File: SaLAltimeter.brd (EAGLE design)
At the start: 100 x 80 mm, 40 parts, among them U1 ATSAMD21G-A, U2 V_REG_LDOSMD, U3 ADXL345

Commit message: added transmiter
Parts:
- added C13: 39pF, SparkFun-Capacitors:0402-CAP
- added C14: 2.2pF, SparkFun-Capacitors:0402-CAP
- added C15, C18, C19: 5.1pF, SparkFun-Capacitors:0402-CAP
- added C16: (no value), SparkFun-Capacitors:0402-CAP
- added C17: 6.2pF, SparkFun-Capacitors:0402-CAP
- added C20, C37: 10nF, SparkFun-Capacitors:0402-CAP
- added C21, C23, C24, C25, C26, C27, C30, C31, C33, C34, C35: 47nF, SparkFun-Capacitors:0402-CAP
- added C22: 1.8nF, SparkFun-Capacitors:0402-CAP
- added C28, C29: 15pF, SparkFun-Capacitors:0402-CAP
- added C32: 220nF, SparkFun-Capacitors:0402-CAP
- added C36: 56pF, SparkFun-Capacitors:0402-CAP
- added C38: 100pF, SparkFun-Capacitors:0402-CAP
- added J$1: SMA_EDGE, SparkFun-Connectors:SMA-EDGE
- added L2, L6: 15nH, SparkFun-Passives:C0402
- added L3: 43nH, SparkFun-Passives:C0402
- added L4: 22nH, SparkFun-Passives:C0402
- added L5, L7: 56nH, SparkFun-Passives:C0402
- added L8, L9: 27nH, SparkFun-Passives:C0402
- added R13, R15: (no value), SparkFun-Passives:0402-RES
- added R14: 0ohm, SparkFun-Passives:0402-RES
- added R16: 56KOhm, SparkFun-Passives:0402-RES
- added S1: SWITCH-MOMENTARY-2SMD-3, SparkFun-Electromechanical:TACTILE_SWITCH_SMD-3
- added U$7: CC1120, SaL-lib:CC1120
- added U4: (no value), adafruit:FGPMMOPA6H
- added Y3: 32MHz, SparkFun-FreqCtrl:CRYSTAL-SMD-5X3
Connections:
- new net CS_TX: U$7.11
- new net N$10: C13.2, C14.1, L2.1
- new net N$11: C14.2, C15.1, L2.2, L3.1
- new net N$12: C16.2, C17.1, L3.2, L4.1
- new net N$13: C16.1, J$1.SIG, L4.2
- new net N$15: C23.2, U$7.25
- new net N$16: C15.2, L6.2, U$7.18
- new net N$17: C18.1, L7.2, L9.1, U$7.19
- new net N$18: C18.2, L6.1, L8.2
- new net N$19: C19.1, L7.1, L8.1, U$7.20
- new net N$20: C22.1, U$7.24
- new net N$21: C22.2, U$7.23
- new net N$22: C20.1, U$7.21
- new net N$23: C24.2, U$7.26
- new net N$24: R16.1, U$7.14
- new net N$25: R14.1, U$7.32
- new net N$26: C27.2, U$7.29
- new net N$27: C29.2, U$7.30, Y3.3
- new net N$28: C28.2, U$7.31, Y3.1
- new net N$34: C32.2, U$7.6
- new net N$38: C36.2, L5.1, R15.1
- new net N$9: C13.1, L5.2, U$7.17
- new net PROG: R13.2, S1.1
- net 3.3V: now also C21.1, C25.2, C26.2, C30.2, C31.2, C33.2, C34.2, C35.2, C36.1, C37.2, C38.2, R15.2, S1.4, U$7.1, U$7.12, U$7.13, U$7.15, U$7.22, U$7.27, U$7.28, U$7.5
- net GND: now also C17.2, C19.2, C20.2, C21.2, C23.1, C24.1, C25.1, C26.1, C27.1, C28.1, C29.1, C30.1, C31.1, C32.1, C33.1, C34.1, C35.1, C37.1, C38.1, J$1.GND@0, J$1.GND@1, J$1.GND@2, J$1.GND@3, L9.2, R13.1, R14.2, R16.2
- net MISO: now also U$7.9
- net MOSI: now also U$7.7
- net SCK: now also U$7.8
- net SWCLK: now also U1.45
- net SWDIO: now also U1.46
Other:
- board size 100 x 80 mm -> 244.8 x 151.1 mm

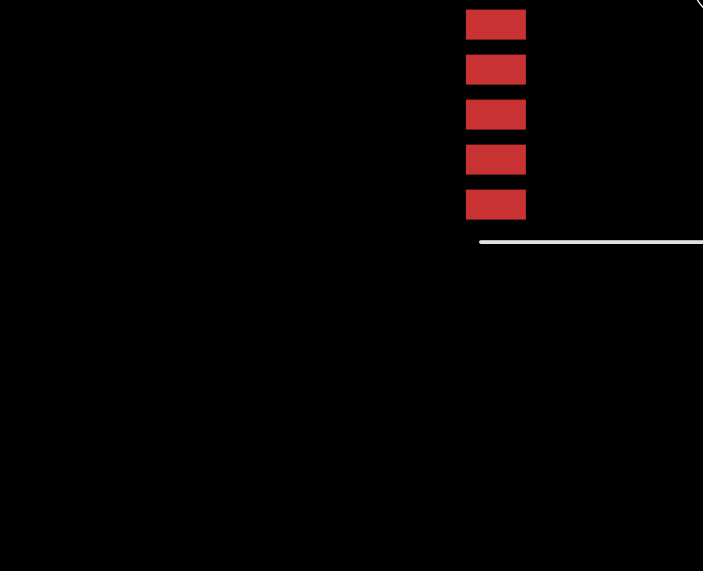
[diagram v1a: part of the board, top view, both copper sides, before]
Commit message: fixed gps
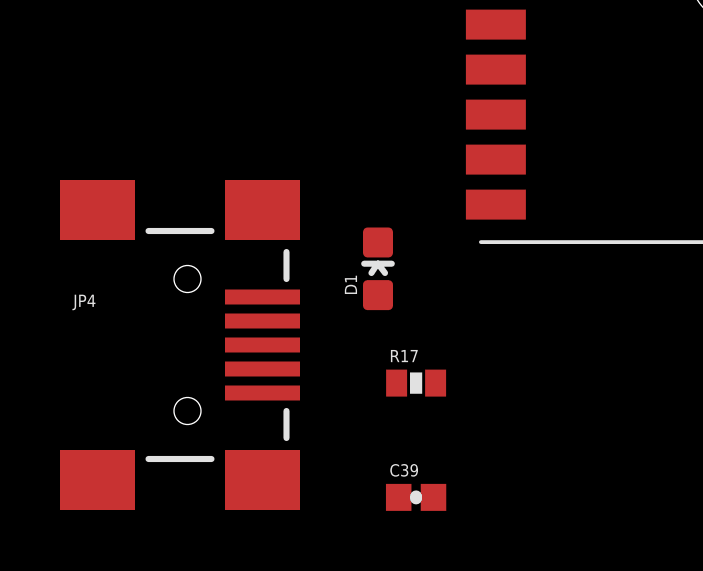
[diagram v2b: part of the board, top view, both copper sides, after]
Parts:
- added C39: 0.1uF, SparkFun-Capacitors:0402-CAP
- added D1: RED, SparkFun-LED:LED-0603
- added JP4: USBSMD, SparkFun-Connectors:USB-MINIB
- added R17: 301ohm\, SparkFun-Passives:0402-RES
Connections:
- new net N$30: D1.C, R17.2
- new net N$31: D1.A, U4.P$5
- new net RX_GPS: U4.P$9
- new net TX_GPS: U4.P$10
- net 3.3V: now also C39.2, U4.P$1
- net GND: now also C39.1, R17.1, U4.P$12, U4.P$19, U4.P$3, U4.P$8
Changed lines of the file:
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@@
 <element name="J$1" library="SparkFun-Connectors" package="SMA-EDGE" value="SMA_EDGE" x="-153.67" y="-180.34"/>
 <element name="U4" library="adafruit" package="FGPMMOPA6H" value="" x="-165.1" y="-171.45"/>
+<element name="D1" library="SparkFun-LED" package="LED-0603" value="RED" x="-176.53" y="-180.34">
+<attribute name="PROD_ID" value="DIO-00819" x="-176.53" y="-180.34" size="1.778" layer="27" display="off"/>
+</element>
+<element name="R17" library="SparkFun-Passives" package="0402-RES" value="301ohm\" x="-175.26" y="-184.15"/>
+<element name="C39" library="SparkFun-Capacitors" package="0402-CAP" value="0.1uF" x="-175.26" y="-187.96"/>
+<element name="JP4" library="SparkFun-Connectors" package="USB-MINIB" value="USBSMD" x="-182.88" y="-182.88">
+<attribute name="PROD_ID" value="CONN-08193" x="-182.88" y="-182.88" size="1.778" layer="27" display="off"/>
+</element>
 </elements>
 <signals>
@@
 <contactref element="U$7" pad="12"/>
 <contactref element="C35" pad="2"/>
+<contactref element="U4" pad="P$1"/>
+<contactref element="C39" pad="2"/>
 <wire x1="-154.775" y1="-64.29" x2="-154.775" y2="-66.29" width="0" layer="19" extent="1-1"/>
 <wire x1="-152.15" y1="-63.665" x2="-154.775" y2="-64.29" width="0" layer="19" extent="1-1"/>
@@
 <wire x1="-153.09" y1="-171.45" x2="-153.02" y2="-168.91" width="0" layer="19" extent="1-1"/>
 <wire x1="-153.09" y1="-173.99" x2="-153.09" y2="-171.45" width="0" layer="19" extent="1-1"/>
+<wire x1="-172.6" y1="-164.7" x2="-154.25" y2="-166.37" width="0" layer="19" extent="1-1"/>
+<wire x1="-174.68" y1="-187.96" x2="-172.6" y2="-164.7" width="0" layer="19" extent="1-1"/>
 <wire x1="3.19" y1="8.89" x2="-132.73" y2="-15.24" width="0" layer="19" extent="1-1"/>
 <wire x1="6.97" y1="11.43" x2="3.19" y2="8.89" width="0" layer="19" extent="1-1"/>
@@
 <contactref element="J$1" pad="GND@1"/>
 <contactref element="J$1" pad="GND@0"/>
+<contactref element="U4" pad="P$12"/>
+<contactref element="U4" pad="P$19"/>
+<contactref element="U4" pad="P$3"/>
+<contactref element="U4" pad="P$8"/>
+<contactref element="R17" pad="1"/>
+<contactref element="C39" pad="1"/>
 <wire x1="-146.7" y1="-66.04" x2="-153.09" y2="-83.82" width="0" layer="19" extent="1-1"/>
 <wire x1="-133.35" y1="-63.5508" x2="-146.7" y2="-66.04" width="0" layer="19" extent="1-1"/>
@@
 <wire x1="-154.25" y1="-161.29" x2="-154.25" y2="-158.75" width="0" layer="19" extent="1-1"/>
 <wire x1="-154.25" y1="-163.83" x2="-154.25" y2="-161.29" width="0" layer="19" extent="1-1"/>
-<wire x1="-154.25" y1="-171.45" x2="-154.25" y2="-163.83" width="0" layer="19" extent="1-1"/>
+<wire x1="-157.6" y1="-166.2" x2="-154.25" y2="-163.83" width="0" layer="19" extent="1-1"/>
+<wire x1="-154.25" y1="-171.45" x2="-157.6" y2="-166.2" width="0" layer="19" extent="1-1"/>
 <wire x1="-154.25" y1="-173.99" x2="-154.25" y2="-171.45" width="0" layer="19" extent="1-1"/>
 <wire x1="-153.02" y1="-176.53" x2="-154.25" y2="-173.99" width="0" layer="19" extent="1-1"/>
 <wire x1="-153.67" y1="-180.34" x2="-153.02" y2="-176.53" width="0" layer="19" extent="1-16"/>
 <wire x1="-153.67" y1="-180.34" x2="-153.67" y2="-180.34" width="0" layer="19" extent="1-16"/>
+<wire x1="-157.6" y1="-176.7" x2="-154.25" y2="-173.99" width="0" layer="19" extent="1-1"/>
 <wire x1="-148.59" y1="-180.34" x2="-153.67" y2="-180.34" width="0" layer="19" extent="16-16"/>
 <wire x1="-148.59" y1="-180.34" x2="-148.59" y2="-180.34" width="0" layer="19" extent="1-16"/>
+<wire x1="-172.6" y1="-175.2" x2="-157.6" y2="-176.7" width="0" layer="19" extent="1-1"/>
+<wire x1="-172.6" y1="-167.7" x2="-172.6" y2="-175.2" width="0" layer="19" extent="1-1"/>
+<wire x1="-175.91" y1="-184.15" x2="-172.6" y2="-175.2" width="0" layer="19" extent="1-1"/>
+<wire x1="-175.84" y1="-187.96" x2="-175.91" y2="-184.15" width="0" layer="19" extent="1-1"/>
 <wire x1="8.27" y1="11.43" x2="-131.43" y2="-15.24" width="0" layer="19" extent="1-1"/>
 <wire x1="8.27" y1="13.97" x2="8.27" y2="11.43" width="0" layer="19" extent="1-1"/>
@@
 <contactref element="U$7" pad="11"/>
 </signal>
+<signal name="N$30">
+<contactref element="D1" pad="C"/>
+<contactref element="R17" pad="2"/>
+<wire x1="-176.53" y1="-179.463" x2="-174.61" y2="-184.15" width="0" layer="19" extent="1-1"/>
+</signal>
+<signal name="N$31">
+<contactref element="U4" pad="P$5"/>
+<contactref element="D1" pad="A"/>
+<wire x1="-172.6" y1="-170.7" x2="-176.53" y2="-181.217" width="0" layer="19" extent="1-1"/>
+</signal>
+<signal name="RX_GPS">
+<contactref element="U4" pad="P$9"/>
+</signal>
+<signal name="TX_GPS">
+<contactref element="U4" pad="P$10"/>
+</signal>
 </signals>

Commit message: aligned tx parts
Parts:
- moved J$1 325.8 mm to (86.4, 40.0), turned to 90 degrees
- moved R16 310.7 mm to (66.7, 42.5), turned to 270 degrees
- moved C36 302.2 mm to (47.6, 59.1)
- moved R15 300.9 mm to (46.4, 55.9)
- moved C38 300.8 mm to (47.6, 49.5)
- moved C37 300.4 mm to (46.4, 52.7)
- moved C35 300.0 mm to (64.1, 42.5), turned to 90 degrees
- moved C33 299.4 mm to (67.9, 42.5), turned to 90 degrees
- moved C34 299.2 mm to (65.4, 42.5), turned to 90 degrees
- moved C32 294.7 mm to (60.3, 46.4)
- moved R14 293.9 mm to (61.6, 51.4), turned to 180 degrees
- moved C31 293.8 mm to (60.3, 47.6)
- moved C30 292.9 mm to (60.3, 48.9)
- moved C29 290.0 mm to (61.6, 54.6), turned to 90 degrees
- moved Y3 288.8 mm to (57.8, 54.6)
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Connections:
- removed net MISO: U$4.SO, U$5.6, U$7.9, U3.12
- removed net MOSI: U$4.SI, U$5.7, U$7.7, U3.13
- removed net RX_GPS: U4.P$9
- removed net SCK: U$4.SCK, U$5.8, U$7.8, U3.14
- removed net TX_GPS: U4.P$10
- new net GPS_RX: U1.16, U4.P$9
- new net GPS_TX: U1.15, U4.P$10
- new net SPI_MISO: U$4.SO, U$5.6, U$7.9, U1.21, U3.12
- new net SPI_MOSI: U$4.SI, U$5.7, U$7.7, U1.19, U3.13
- new net SPI_SCK: U$4.SCK, U$5.8, U$7.8, U1.20, U3.14
- net CS_ACCEL: now also U1.24
- net CS_BARO: now also U1.22
- net CS_MEM: now also U1.23
- net CS_TX: now also U1.25
- net PROG: now also U1.26

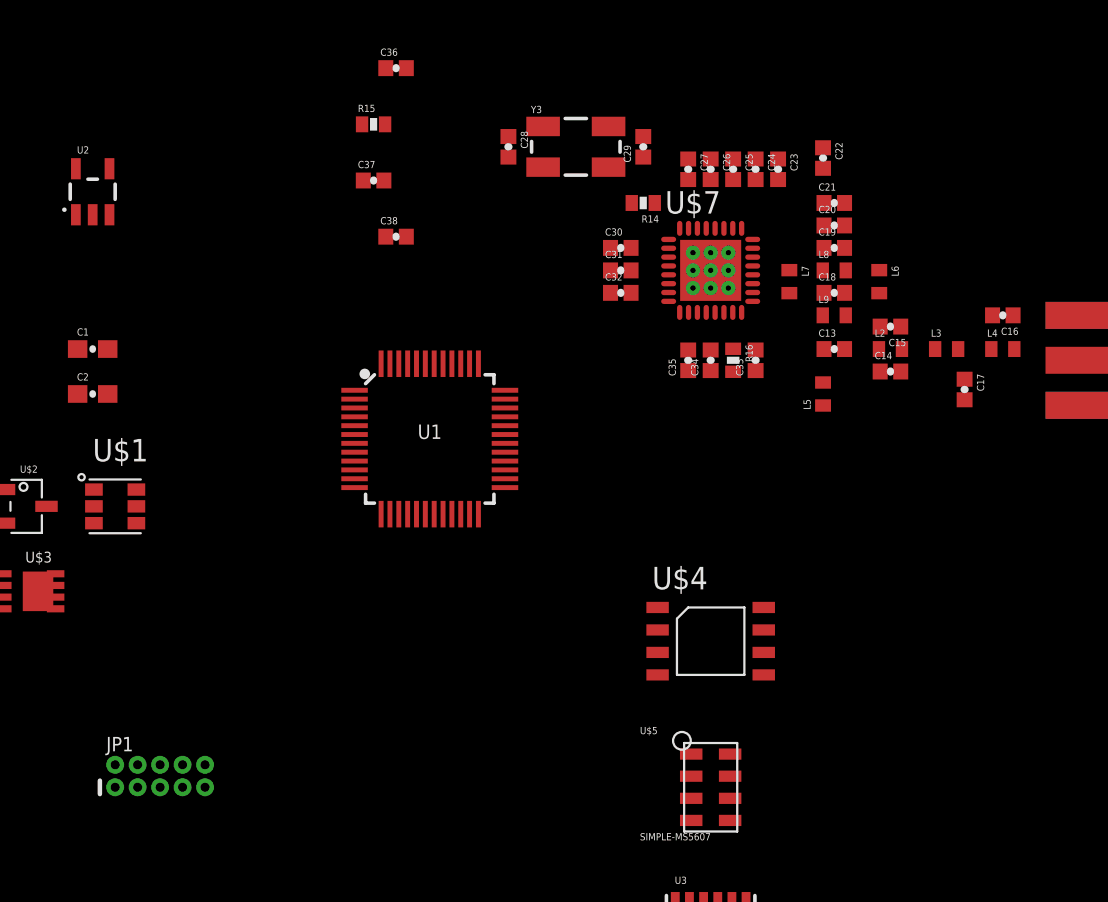
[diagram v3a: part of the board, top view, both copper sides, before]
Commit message: starting 4 layer routing
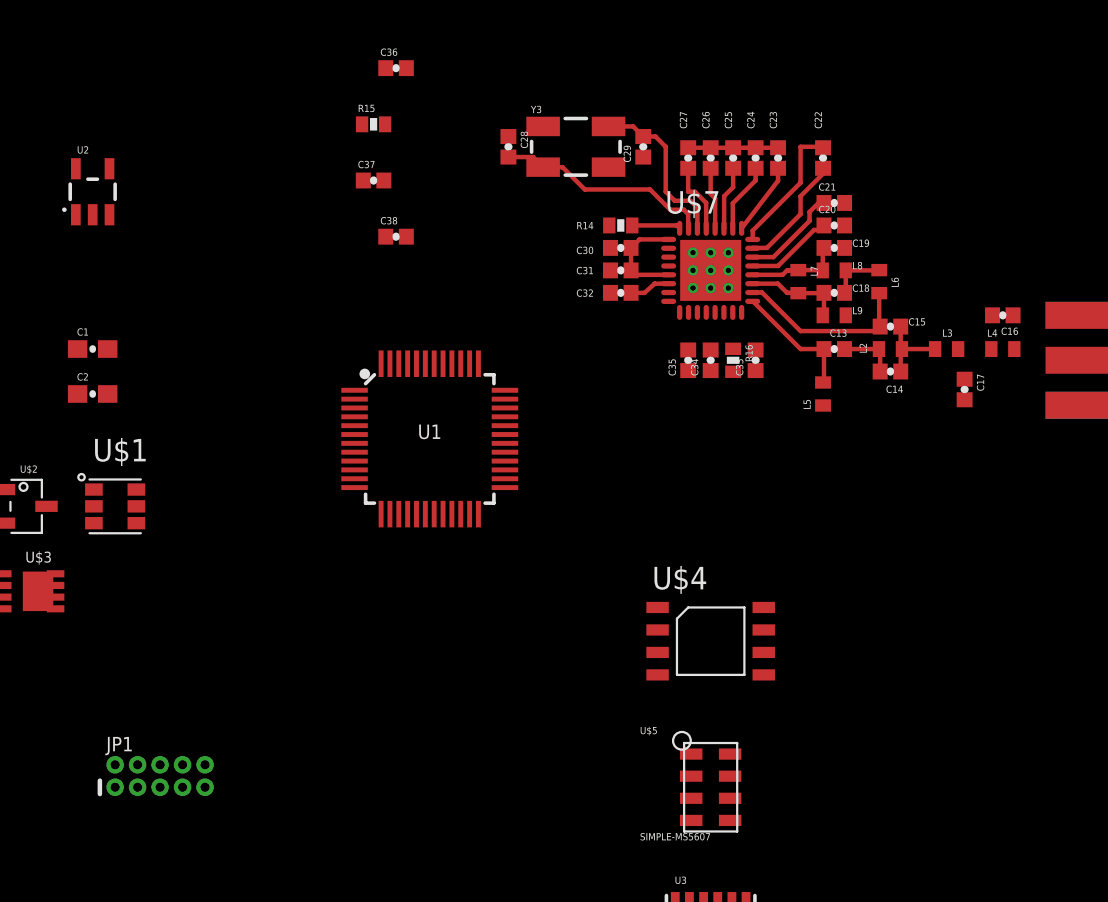
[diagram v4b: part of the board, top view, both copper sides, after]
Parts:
- moved R14 1.80 mm to (60.3, 50.2)
- moved C23 0.63 mm to (69.2, 54.0)
- moved C24 0.63 mm to (67.9, 54.0)
- moved C25 0.63 mm to (66.7, 54.0)
- moved C26 0.63 mm to (65.4, 54.0)
- moved C27 0.63 mm to (64.1, 54.0)
- moved L7 0.51 mm to (70.4, 47.0)
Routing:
- net 3.3V: track 0.00 -> 18.5 mm
- net N$28: track 0.00 -> 12.3 mm
- net N$16: track 0.00 -> 10.1 mm
- net N$27: track 0.00 -> 9.58 mm
- net N$20: track 0.00 -> 7.65 mm
- net N$9: track 0.00 -> 7.06 mm
- net N$21: track 0.00 -> 6.62 mm
- net N$17: track 0.00 -> 5.55 mm
- net N$19: track 0.00 -> 5.37 mm
- net GND: track 0.00 -> 5.08 mm
- net N$22: track 0.00 -> 4.98 mm
- net N$11: track 0.00 -> 4.47 mm
- net N$15: track 0.00 -> 4.09 mm
- net N$26: track 0.00 -> 4.04 mm
- net N$23: track 0.00 -> 3.93 mm
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
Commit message: lots of work on the layout
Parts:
- R10, R11, R12, R5, R6, R7, R8, R9: value (none) -> 10kohm; device SparkFun-Passives:0603-RES -> SparkFun-Resistors:0402-RES
- moved U4 258.6 mm to (19.7, 9.53), flipped to the bottom, turned to 270 degrees
- moved C39 258.6 mm to (17.1, -15.2)
- moved D1 258.6 mm to (15.9, -7.62)
- moved JP4 258.6 mm to (9.53, -10.2)
- moved R17 258.6 mm to (17.1, -11.4)
- moved R13 209.4 mm to (55.2, -8.26)
- moved S1 184.1 mm to (29.8, -11.4)
- moved R2 176.2 mm to (41.9, 1.27), turned to 180 degrees
- moved C12 175.8 mm to (37.5, 12.1), turned to 180 degrees
- moved C11 173.4 mm to (37.5, 13.3), turned to 180 degrees
- moved C9 171.2 mm to (38.4, 1.27)
- moved R4 170.3 mm to (33.0, 10.2), turned to 90 degrees
- moved JP2 167.8 mm to (9.91, 15.1), flipped to the bottom
- moved JP3 166.7 mm to (7.24, 4.57), flipped to the bottom, turned to 180 degrees
- moved R3 165.7 mm to (30.7, 1.40), turned to 180 degrees
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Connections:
- net FET_A: now also R9.2; no longer R9.1
- net FET_B: now also R11.1; no longer R11.2
- net FIRE_A: now also R5.2, R6.1, U1.28; no longer R5.1, R6.2
- net FIRE_B: now also U1.30
- net GND: now also R10.1, R12.2, R5.1; no longer R10.2, R12.1, R6.1
- net N$1: now also R6.2; no longer R5.2
- net SENSE_A: now also R10.2, R9.1, U1.27; no longer R10.1, R9.2
- net SENSE_B: now also R11.2, R12.1, U1.29; no longer R11.1, R12.2
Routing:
- net 3.3V: track 18.5 -> 28.4 mm
- net N$12: track 0.00 -> 5.38 mm
- net N$13: track 0.00 -> 3.16 mm
- net N$20: track 7.65 -> 4.86 mm
- net N$38: track 0.00 -> 2.59 mm
- net GND: track 5.08 -> 7.56 mm
- net N$24: track 0.00 -> 2.27 mm
- net N$27: track 9.58 -> 7.63 mm
- net N$26: track 4.04 -> 2.71 mm
- net N$23: track 3.93 -> 2.81 mm
- net N$28: track 12.3 -> 11.3 mm
- net N$15: track 4.09 -> 3.11 mm
- net N$21: track 6.62 -> 6.08 mm
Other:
- board size 244.8 x 151.1 mm -> 76.5 x 19.7 mm

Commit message: squished it all inside
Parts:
- moved L1 82.7 mm to (15.9, 6.35), turned to 270 degrees
- moved C3 79.9 mm to (14.2, 6.35), turned to 90 degrees
- moved C4 73.7 mm to (14.6, 10.2), turned to 90 degrees
- moved C5 71.5 mm to (15.9, 10.2), turned to 270 degrees
- moved R1 62.7 mm to (28.6, 16.5), turned to 270 degrees
- moved C8 61.6 mm to (20.3, 14.0), turned to 90 degrees
- moved JP4 54.8 mm to (59.1, 13.3), flipped to the bottom, turned to 270 degrees
- moved S1 23.1 mm to (48.3, 2.54), flipped to the bottom
- moved R17 21.1 mm to (33.0, 2.54), flipped to the bottom
- moved C39 20.1 mm to (27.4, 2.03), turned to 180 degrees
- moved D1 17.3 mm to (29.8, 2.54), flipped to the bottom, turned to 90 degrees
- moved R13 11.4 mm to (51.4, 2.54), flipped to the bottom, turned to 90 degrees
- moved U$3 7.48 mm to (2.92, 9.27), turned to 270 degrees
- moved R5 6.19 mm to (8.51, 12.8)
- moved R6 6.19 mm to (7.11, 12.8), turned to 270 degrees
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
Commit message: starting wiring
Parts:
- removed C16: (no value), SparkFun-Capacitors:0402-CAP
- removed S1: SWITCH-MOMENTARY-2SMD-3, SparkFun-Electromechanical:TACTILE_SWITCH_SMD-3
- added F1: PTCSMD, SparkFun-PowerIC:PTC-1206
- added S2: SWITCH-MOMENTARY-2SMD-4.6X2.8MM, SparkFun-Electromechanical:TACTILE_SWITCH_SMD_4.6X2.8MM
- added SG1: BUZZERSMD2, SparkFun-Electromechanical:BUZZER-CCV
- added STANDOFF1, STANDOFF2, STANDOFF3: STAND-OFF, SparkFun-Electromechanical:STAND-OFF
- JP4: value USBSMD -> USB-MICROB; device SparkFun-Connectors:USB-MINIB -> SparkFun-Connectors:USB-MICROB
- moved U$2 12.1 mm to (3.17, 14.6), flipped to the bottom, turned to 270 degrees
- moved C8 7.67 mm to (27.6, 16.5)
- moved C4 7.44 mm to (20.6, 14.6), turned to 135 degrees
- moved R6 6.70 mm to (13.1, 9.78), turned to 180 degrees
- moved R7 6.23 mm to (13.1, 8.26), turned to 0 degrees
- moved C5 5.21 mm to (19.7, 13.7), turned to 135 degrees
- moved U$1 5.08 mm to (4.45, 2.54), flipped to the top, turned to 180 degrees
- moved R5 4.86 mm to (13.1, 11.2), turned to 0 degrees
- moved R8 4.70 mm to (13.1, 6.86), turned to 180 degrees
- moved C2 4.26 mm to (15.2, 17.8), turned to 180 degrees
- moved JP4 3.81 mm to (59.1, 17.1), turned to 180 degrees
- moved L1 3.78 mm to (13.1, 3.81), turned to 180 degrees
- moved C6 3.56 mm to (17.8, 6.10), turned to 225 degrees
- moved JP2 3.30 mm to (6.60, 15.1), flipped to the top
- moved C1 2.90 mm to (15.9, 12.6), turned to 0 degrees
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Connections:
- new net BUZZER: SG1.-, U1.27
- new net N$14: F1.1, JP4.VBUS
- new net SENSE_BAT: U1.9
- new net USB_D+: JP4.D+, U1.34
- new net USB_D-: JP4.D-, U1.33
- net 3.3V: now also S2.3, S2.4; no longer S1.4
- net FIRE_A: now also U1.45; no longer U1.28
- net FIRE_B: now also U1.46; no longer U1.30
- net GND: now also JP4.GND, JP4.MT1, JP4.MT2, SG1.+
- net N$12: no longer C16.2
- net N$13: no longer C16.1
- net PROG: now also S2.1, S2.2; no longer S1.1
- net SENSE_A: now also U1.7; no longer U1.27
- net SENSE_B: now also U1.8; no longer U1.29
- net SWCLK: no longer U1.45
- net SWDIO: no longer U1.46
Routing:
- net GND: track 7.56 -> 84.1 mm, vias 0 -> 20
- net 3.3V: track 28.4 -> 71.2 mm, vias 0 -> 8
- net LVD_IN: track 0.00 -> 36.9 mm, vias 0 -> 4
- net RAW: track 0.00 -> 35.8 mm, vias 0 -> 5
- net N$2: track 0.00 -> 25.5 mm, vias 0 -> 1
- net SENSE_A: track 0.00 -> 22.6 mm, vias 0 -> 2
- net SENSE_B: track 0.00 -> 15.5 mm, vias 0 -> 2
- net !RESET: track 0.00 -> 12.4 mm
- net FIRE_B: track 0.00 -> 11.7 mm
- net FIRE_A: track 0.00 -> 10.7 mm
- net GATE: track 0.00 -> 8.69 mm
- net N$1: track 0.00 -> 7.57 mm, vias 0 -> 2
- net FET_B: track 0.00 -> 6.17 mm
- net N$4: track 0.00 -> 5.88 mm
- net N$8: track 0.00 -> 5.70 mm, vias 0 -> 2
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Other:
- board size 76.5 x 19.7 mm -> 74.6 x 19.7 mm

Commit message: more wiring
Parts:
- moved FRAME1 97.1 mm to (-5.08, 23.5)
- moved D1 18.3 mm to (19.7, 17.8), flipped to the top, turned to 270 degrees
- moved R17 18.3 mm to (22.9, 17.8), flipped to the top, turned to 180 degrees
- moved U$6 0.63 mm to (7.37, 10.3)
- moved C8 0.63 mm to (28.2, 16.5)
- moved JP2 0.36 mm to (6.86, 14.9)
- moved J1 0.13 mm to (-0.76, 10.2)
- moved R12 0.13 mm to (9.53, 1.91)
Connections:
- net CS_TX: now also U1.28; no longer U1.25
- net GPS_RX: now also U1.38; no longer U1.16
- net GPS_TX: now also U1.37; no longer U1.15
- net PROG: now also U1.29; no longer U1.26
- net SPI_MISO: now also U1.25
- net SPI_MOSI: now also U1.26
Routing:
- net GND: track 84.1 -> 121.0 mm, vias 20 -> 23
- net 3.3V: track 71.2 -> 81.4 mm, vias 8 -> 9
- net GPS_RX: track 0.00 -> 4.82 mm, vias 0 -> 1
- net GPS_TX: track 0.00 -> 3.59 mm, vias 0 -> 1
- net FET_A: track 4.51 -> 6.49 mm
- net SENSE_A: track 22.6 -> 23.6 mm
- net FET_B: track 6.17 -> 5.55 mm
- net N$1: track 7.57 -> 8.16 mm
- net !RESET: track 12.4 -> 12.7 mm, vias 0 -> 1
